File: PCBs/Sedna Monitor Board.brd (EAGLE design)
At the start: 160 x 100 mm, 39 parts, among them J1 uC Connection

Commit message: Started working on the Monitor Board layout
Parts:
- moved CFILT1_5V 219.4 mm to (59.2, 47.4)
- moved CFILT2_5V 209.2 mm to (59.2, 42.2), turned to 180 degrees
- moved RFILT2_5V 205.9 mm to (59.2, 44.8)
- moved RFILT1_5V 202.9 mm to (64.0, 44.8)
- moved CFILT1_7.8V 183.3 mm to (59.2, 31.0)
- moved CFILT2_7.8V 182.4 mm to (59.2, 36.2), turned to 180 degrees
- moved RFILT2_7.8V 175.0 mm to (59.2, 33.6)
- moved RFILT1_7.8V 172.7 mm to (64.0, 33.6)
- moved CFILT1_12V 153.3 mm to (43.2, 31.0)
- moved CFILT2_12V 152.4 mm to (43.2, 36.2)
- moved RFILT2_12V 145.0 mm to (43.2, 33.6), turned to 180 degrees
- moved CFILT1_VIN 141.8 mm to (43.2, 47.4)
- moved CFILT2_VIN 141.7 mm to (43.2, 42.2)
- moved RL_5V 138.5 mm to (64.0, 42.2), turned to 180 degrees
- moved RFILT1_12V 137.1 mm to (38.4, 33.6), turned to 180 degrees
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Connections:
- net N$24: now also ADC.5; no longer ADC.2
- net N$4: now also ADC.1; no longer ADC.5
- net N$5: now also ADC.2; no longer ADC.1
- net N$8: now also ADC.4; no longer ADC.3
- net N$9: now also ADC.3; no longer ADC.4
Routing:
- net N$24: track 0.00 -> 59.6 mm
- net N$5: track 0.00 -> 53.8 mm
- net N$8: track 0.00 -> 50.2 mm
- net N$9: track 0.00 -> 45.0 mm
- net GND: track 17.4 -> 44.1 mm, vias 0 -> 2
- net N$18: track 0.00 -> 7.76 mm
- net N$16: track 0.00 -> 7.67 mm
- net N$25: track 0.00 -> 7.67 mm
- net N$12: track 0.00 -> 7.67 mm
- net N$23: track 0.00 -> 5.50 mm
- net N$21: track 0.00 -> 5.50 mm
- net N$17: track 0.00 -> 5.50 mm
- net N$13: track 0.00 -> 5.50 mm
- net N$3: track 0.00 -> 5.45 mm
- net N$14: track 0.00 -> 5.45 mm
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
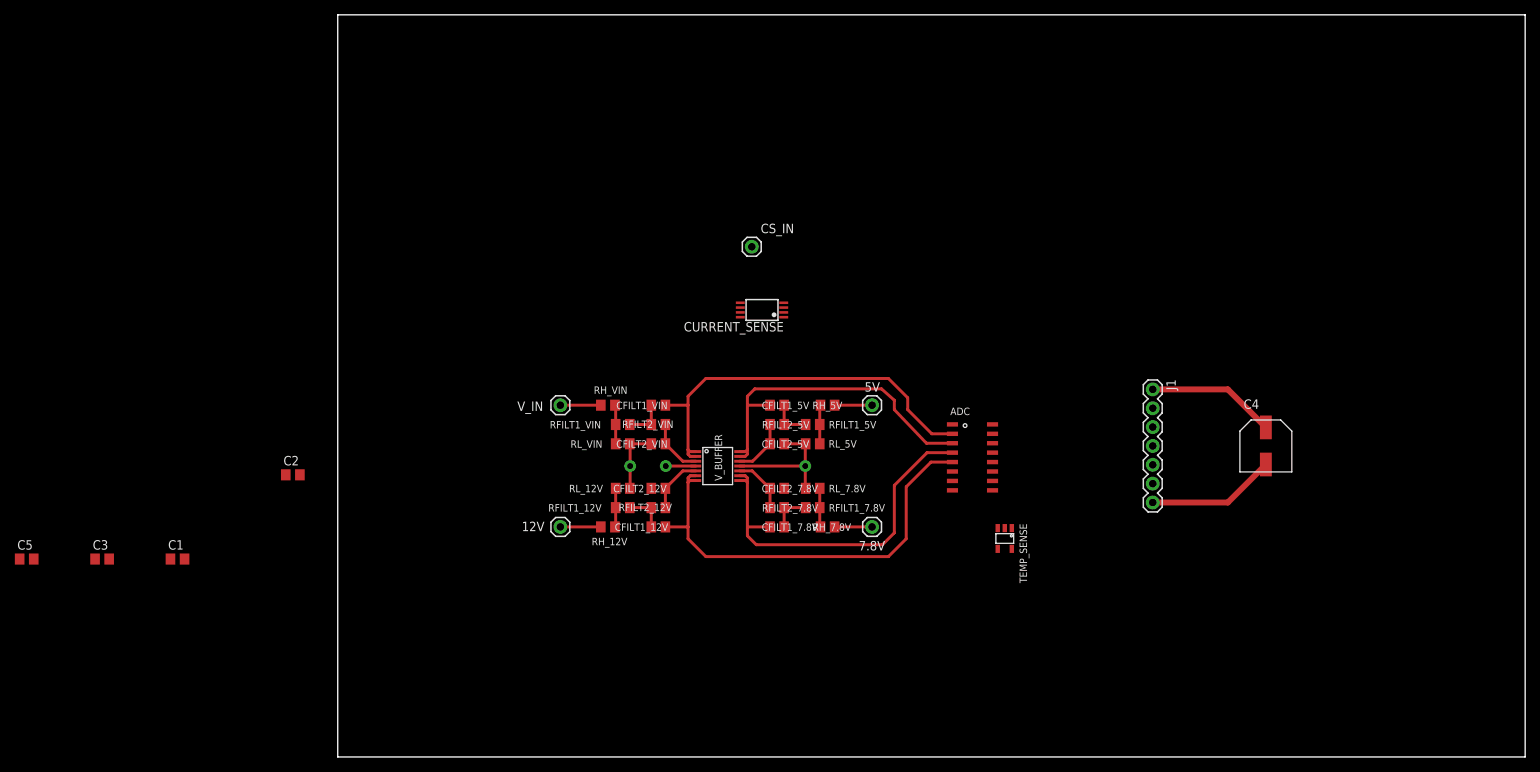
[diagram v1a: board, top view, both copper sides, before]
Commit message: Finished the Monitor Board v1.0
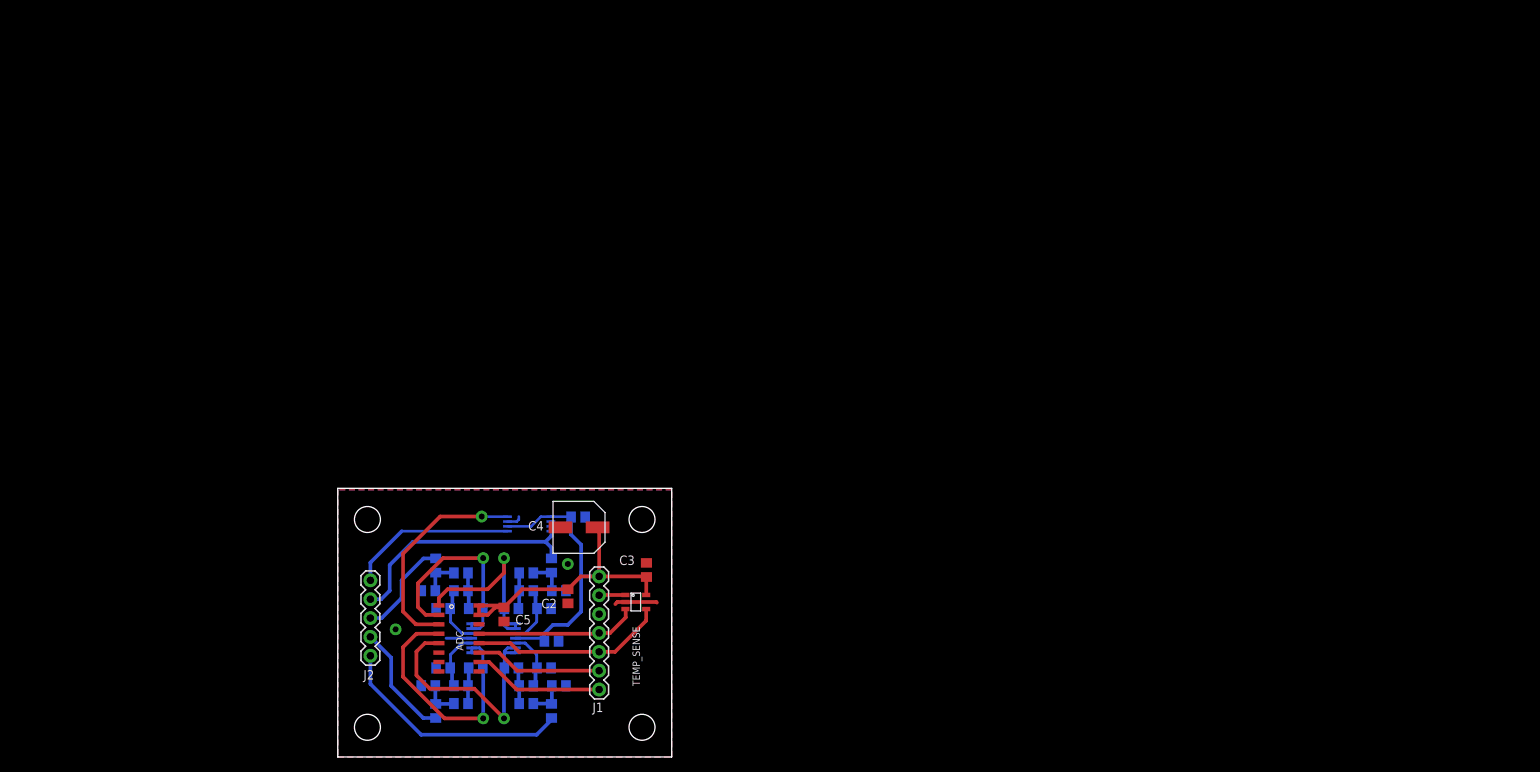
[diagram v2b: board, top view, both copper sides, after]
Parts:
- removed 12V, 5V, 7.8V, CS_IN, V_IN: (no value), SparkFun-Connectors:1X01
- added C6: 0.1uF, 50V, rcl:C0805
- added J2: Rail Header, Sedna Components:1X05
- moved C4 93.2 mm to (32.5, 30.9), turned to 270 degrees
- moved J1 78.7 mm to (35.2, 24.3)
- moved ADC 73.4 mm to (16.3, 16.0)
- moved C3 73.4 mm to (41.6, 25.2), turned to 90 degrees
- moved C5 64.7 mm to (22.4, 19.2), turned to 270 degrees
- moved RH_7.8V 58.3 mm to (13.2, 6.20), flipped to the bottom, turned to 270 degrees
- moved RL_7.8V 58.2 mm to (12.2, 9.60), flipped to the bottom, turned to 180 degrees
- moved RH_5V 57.0 mm to (13.2, 25.8), flipped to the bottom, turned to 270 degrees
- moved RL_5V 55.5 mm to (12.2, 22.4), flipped to the bottom, turned to 0 degrees
- moved C1 54.3 mm to (32.4, 32.3), flipped to the bottom, turned to 180 degrees
- moved RFILT1_7.8V 54.3 mm to (16.6, 7.20), flipped to the bottom
- moved RFILT1_5V 51.4 mm to (16.6, 24.8), flipped to the bottom
- moved CFILT2_7.8V 51.1 mm to (14.2, 12.0), flipped to the bottom
- moved TEMP_SENSE 50.5 mm to (40.2, 20.9), turned to 0 degrees
- moved CFILT2_5V 50.2 mm to (14.2, 20.0), flipped to the bottom
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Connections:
- net N$24 renamed VOUT_B
- net N$6 renamed MOSI
- net N$8 renamed VOUT_C
- removed net N$20: 7.8V.1, RH_7.8V.2
- removed net N$5: ADC.2, CFILT1_VIN.2, V_BUFFER.1, V_BUFFER.2
- removed net N$9: ADC.3, CFILT1_5V.1, V_BUFFER.13, V_BUFFER.14
- new net CS_OUT: ADC.3, CURRENT_SENSE.4
- new net VOUT_A: ADC.1, CFILT1_VIN.2, V_BUFFER.1, V_BUFFER.2
- new net VOUT_D: ADC.2, CFILT1_5V.1, V_BUFFER.13, V_BUFFER.14
- net ADC_CS: now also J1.7; no longer J1.3
- net GND: now also C6.2, J1.3; no longer J1.7
- net N$10: now also J2.3; no longer 5V.1
- net N$14: now also J2.5; no longer 12V.1
- net N$2: now also J2.1; no longer CS_IN.1
- net N$3: now also J2.2; no longer V_IN.1
- net N$4: now also J2.4, RH_7.8V.2; no longer ADC.1, CURRENT_SENSE.4
- net VDD: now also C6.1
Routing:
- net N$5: track 53.8 -> 0.00 mm
- net VDD: track 21.4 -> 74.8 mm, vias 1 -> 0
- net N$9: track 45.0 -> 0.00 mm
- net GND: track 44.1 -> 13.2 mm
- net VOUT_D: track 0.00 -> 29.6 mm, vias 0 -> 1
- net CS_OUT: track 0.00 -> 29.5 mm, vias 0 -> 1
- net N$3: track 5.45 -> 33.2 mm
- net N$14: track 5.45 -> 32.1 mm
- net N$1: track 0.00 -> 26.3 mm
- net VOUT_A: track 0.00 -> 26.2 mm, vias 0 -> 1
- net VOUT_B: track 59.6 -> 33.8 mm, vias 0 -> 1
- net N$2: track 0.00 -> 22.6 mm
- net SCK: track 0.00 -> 21.8 mm
- net ADC_CS: track 0.00 -> 17.7 mm
- net MOSI: track 0.00 -> 17.2 mm
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- added copper zone on layer 1, net GND
- added copper zone on layer 16, net GND
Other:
- board size 160 x 100 mm -> 45 x 36.2 mm
- board text added: "Sedna Monitor Board v1.0"
